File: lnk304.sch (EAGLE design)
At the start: 25 parts, among them IC2 MCP1703CB

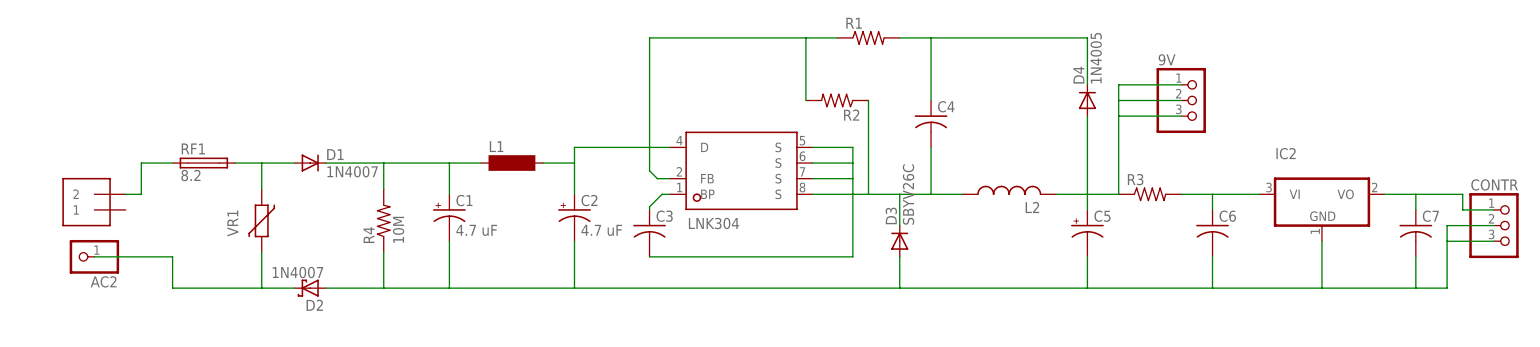
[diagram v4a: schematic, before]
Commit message: Added passive componets' values which were removed by mistake
** 27.Mar.2016 **

Schematic:
- Added passive componets' values which were removed by mistake

PCB Layout:
- Smash passive components and remove passive components' values

-- Missing --
- Need to add hot and neutral pins for AC plug concept
- Need to revise Terminal Block size and overlapping with D2
- May need to increase L2 pad distance a bit
- May need to decrease the board height by 2mm
- Add Creepage between C1 and C2 pads
- Revise the two holes diameter and availability of screws
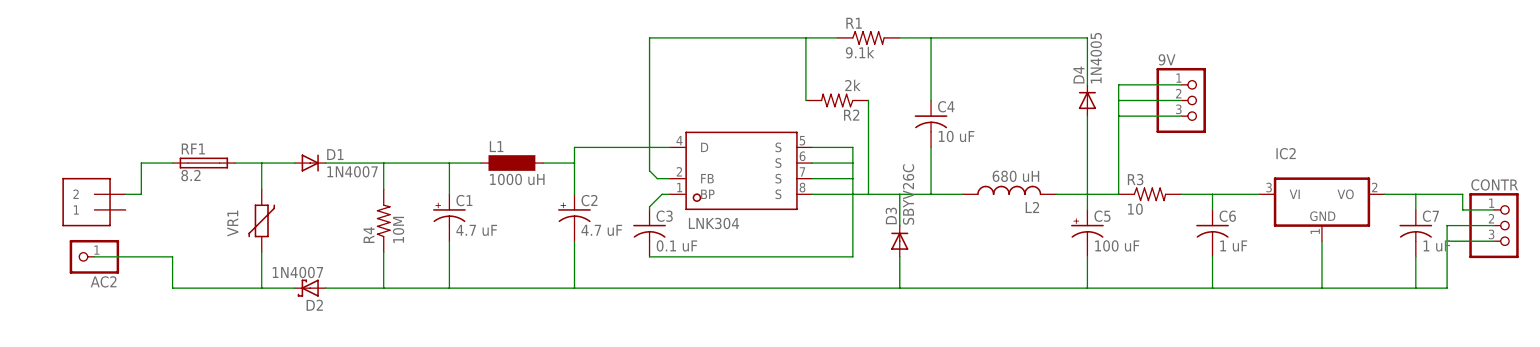
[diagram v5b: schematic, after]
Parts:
- C3: value (none) -> 0.1 uF
- C4: value (none) -> 10 uF
- C5: value (none) -> 100 uF
- C6, C7: value (none) -> 1 uF
- L1: value (none) -> 1000 uH
- L2: value (none) -> 680 uH
- R1: value (none) -> 9.1k
- R2: value (none) -> 2k
- R3: value (none) -> 10
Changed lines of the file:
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@@
 <part name="C1" library="adafruit" deviceset="CPOL-US" device="E5-10.5" value="4.7 uF"/>
 <part name="C2" library="adafruit" deviceset="CPOL-US" device="E5-10.5" value="4.7 uF"/>
-<part name="L1" library="inductor-neosid" deviceset="BS" device="11"/>
-<part name="C4" library="adafruit" deviceset="C-US" device="C0603"/>
-<part name="C3" library="adafruit" deviceset="C-US" device="C0603"/>
+<part name="L1" library="inductor-neosid" deviceset="BS" device="11" value="1000 uH"/>
+<part name="C4" library="adafruit" deviceset="C-US" device="C0603" value="10 uF"/>
+<part name="C3" library="adafruit" deviceset="C-US" device="C0603" value="0.1 uF"/>
 <part name="D3" library="adafruit" deviceset="1N4004" device="" value="SBYV26C"/>
 <part name="D4" library="adafruit" deviceset="1N4004" device="" value="1N4005"/>
-<part name="C5" library="adafruit" deviceset="CPOL-US" device="E2-4"/>
-<part name="L2" library="rcl" deviceset="L-US" device="L5650M"/>
-<part name="R1" library="adafruit" deviceset="R-US_" device="R0603"/>
-<part name="R2" library="adafruit" deviceset="R-US_" device="R0603"/>
+<part name="C5" library="adafruit" deviceset="CPOL-US" device="E2-4" value="100 uF"/>
+<part name="L2" library="rcl" deviceset="L-US" device="L5650M" value="680 uH"/>
+<part name="R1" library="adafruit" deviceset="R-US_" device="R0603" value="9.1k"/>
+<part name="R2" library="adafruit" deviceset="R-US_" device="R0603" value="2k"/>
 <part name="IC2" library="linear" deviceset="MCP1703" device="CB" value=""/>
-<part name="R3" library="adafruit" deviceset="R-US_" device="R1206"/>
-<part name="C6" library="adafruit" deviceset="C-US" device="C0603"/>
-<part name="C7" library="adafruit" deviceset="C-US" device="C0603"/>
+<part name="R3" library="adafruit" deviceset="R-US_" device="R1206" value="10"/>
+<part name="C6" library="adafruit" deviceset="C-US" device="C0603" value="1 uF"/>
+<part name="C7" library="adafruit" deviceset="C-US" device="C0603" value="1 uF"/>
 <part name="AC" library="adafruit" deviceset="1X2" device="-3.5MM"/>
 <part name="AC2" library="adafruit" deviceset="PINHD-1X1" device=""/>

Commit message: Create new PCB layout for AC TBlock and L2
** 8.Apr.2016 **
Created new devices in the library

Schematic:
- Created new library for AC plug
- Added hot and neutral pins for AC plug concept

PCB Layout:
- Revised Terminal Block size and overlapping with D2
- Probably won't need to decrease the board height by 2mm
- Neglect creepage between C1 and C2 pads at the moment
- Increased L2 pad distance a bit by creating a new library ELL-6UH681M
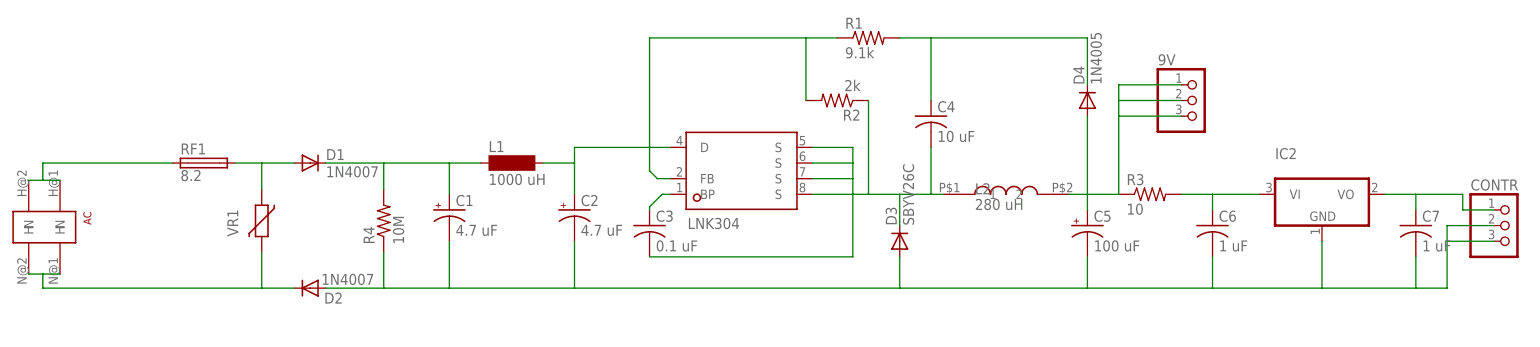
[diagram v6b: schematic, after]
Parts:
- removed AC2: (no value), adafruit:PINHD-1X1
- AC: value 1X2-3.5MM -> TBLOCK02X2; device adafruit:1X2-3.5MM -> userdefined:TBLOCK02X2
- D2: device adafruit:SCHOTTKY-DIODEDO41-7 -> adafruit:1N4004
- L2: value 680 uH -> 280 uH; device rcl:L-USL5650M -> userdefined:ELL-6UH681M
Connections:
- removed net N$9: AC.2, RF1.1
- new net N$12: AC.H@1, AC.H@2, RF1.1
- net N$6: now also AC.N@1, AC.N@2; no longer AC2.1
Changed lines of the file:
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@@
 <part name="RF1" library="fuse" deviceset="FUSE" device="PICOFUSE" value="8.2"/>
 <part name="D1" library="adafruit" deviceset="1N4004" device="" value="1N4007"/>
-<part name="D2" library="adafruit" deviceset="SCHOTTKY-DIODE" device="DO41-7" value="1N4007"/>
+<part name="D2" library="adafruit" deviceset="1N4004" device="" value="1N4007"/>
 <part name="C1" library="adafruit" deviceset="CPOL-US" device="E5-10.5" value="4.7 uF"/>
 <part name="C2" library="adafruit" deviceset="CPOL-US" device="E5-10.5" value="4.7 uF"/>
@@
 <part name="D4" library="adafruit" deviceset="1N4004" device="" value="1N4005"/>
 <part name="C5" library="adafruit" deviceset="CPOL-US" device="E2-4" value="100 uF"/>
-<part name="L2" library="rcl" deviceset="L-US" device="L5650M" value="680 uH"/>
 <part name="R1" library="adafruit" deviceset="R-US_" device="R0603" value="9.1k"/>
 <part name="R2" library="adafruit" deviceset="R-US_" device="R0603" value="2k"/>
@@
 <part name="C6" library="adafruit" deviceset="C-US" device="C0603" value="1 uF"/>
 <part name="C7" library="adafruit" deviceset="C-US" device="C0603" value="1 uF"/>
-<part name="AC" library="adafruit" deviceset="1X2" device="-3.5MM"/>
-<part name="AC2" library="adafruit" deviceset="PINHD-1X1" device=""/>
 <part name="CONTR" library="adafruit" deviceset="PINHD-1X3" device=""/>
 <part name="9V" library="adafruit" deviceset="PINHD-1X3" device=""/>
@@
 <part name="R4" library="resistor" deviceset="R-US_" device="R1206" value="10M"/>
 <part name="VR1" library="varistor" deviceset="VARISTOR" device="-7,5" value=""/>
+<part name="AC" library="userdefined" deviceset="TBLOCK02X2" device=""/>
+<part name="L2" library="userdefined" deviceset="ELL-6UH681M" device="" value="280 uH"/>
 </parts>
 <sheets>
@@
 <instance part="RF1" gate="G$1" x="0.508" y="60.96"/>
 <instance part="D1" gate="1" x="17.78" y="60.96"/>
-<instance part="D2" gate="G$1" x="17.78" y="40.64" rot="R180"/>
+<instance part="D2" gate="1" x="17.78" y="40.64" smashed="yes" rot="R180">
+<attribute name="NAME" x="23.114" y="39.9034" size="1.778" layer="95" rot="R180"/>
+<attribute name="VALUE" x="28.194" y="42.9514" size="1.778" layer="96" rot="R180"/>
+</instance>
 <instance part="C1" gate="G$1" x="40.386" y="53.34"/>
 <instance part="C2" gate="G$1" x="60.706" y="53.34"/>
@@
 <instance part="D4" gate="1" x="144.018" y="71.12" rot="R90"/>
 <instance part="C5" gate="G$1" x="144.018" y="50.8"/>
-<instance part="L2" gate="G$1" x="131.318" y="55.88" rot="R90"/>
 <instance part="R1" gate="G$1" x="108.458" y="81.28"/>
 <instance part="R2" gate="G$1" x="103.378" y="71.12" rot="R180"/>
@@
 <instance part="C6" gate="G$1" x="164.338" y="50.8"/>
 <instance part="C7" gate="G$1" x="197.358" y="50.8"/>
-<instance part="AC" gate="G$1" x="-17.272" y="55.88" rot="R180"/>
-<instance part="AC2" gate="G$1" x="-19.812" y="45.72" rot="R180"/>
 <instance part="CONTR" gate="A" x="212.598" y="50.8"/>
 <instance part="9V" gate="A" x="161.798" y="71.12"/>
@@
 <instance part="R4" gate="G$1" x="29.718" y="51.562" rot="R90"/>
 <instance part="VR1" gate="G$1" x="9.906" y="51.562" rot="R90"/>
+<instance part="AC" gate="G$1" x="-25.4" y="50.546" rot="R270"/>
+<instance part="L2" gate="G$1" x="130.81" y="55.88"/>
 </instances>
 <busses>
@@
 <net name="N$6" class="0">
 <segment>
-<pinref part="D2" gate="G$1" pin="C"/>
+<pinref part="D2" gate="1" pin="C"/>
 <wire x1="15.24" y1="40.64" x2="9.906" y2="40.64" width="0.1524" layer="91"/>
-<pinref part="AC2" gate="G$1" pin="1"/>
-<wire x1="9.906" y1="40.64" x2="-4.572" y2="40.64" width="0.1524" layer="91"/>
-<wire x1="-17.272" y1="45.72" x2="-4.572" y2="45.72" width="0.1524" layer="91"/>
-<wire x1="-4.572" y1="45.72" x2="-4.572" y2="40.64" width="0.1524" layer="91"/>
 <pinref part="VR1" gate="G$1" pin="2"/>
 <wire x1="9.906" y1="46.482" x2="9.906" y2="40.64" width="0.1524" layer="91"/>
+<wire x1="-25.654" y1="40.64" x2="9.906" y2="40.64" width="0.1524" layer="91"/>
+<pinref part="AC" gate="G$1" pin="N@2"/>
+<pinref part="AC" gate="G$1" pin="N@1"/>
+<wire x1="-22.86" y1="42.926" x2="-25.654" y2="42.926" width="0.1524" layer="91"/>
+<wire x1="-25.654" y1="42.926" x2="-27.94" y2="42.926" width="0.1524" layer="91"/>
+<wire x1="-25.654" y1="40.64" x2="-25.654" y2="42.926" width="0.1524" layer="91"/>
 </segment>
 </net>
@@
 <segment>
 <pinref part="D3" gate="1" pin="A"/>
-<pinref part="D2" gate="G$1" pin="A"/>
+<pinref part="D2" gate="1" pin="A"/>
 <pinref part="C2" gate="G$1" pin="-"/>
 <wire x1="60.706" y1="48.26" x2="60.706" y2="40.64" width="0.1524" layer="91"/>
@@
 <net name="N$4" class="0">
 <segment>
-<pinref part="L2" gate="G$1" pin="2"/>
 <pinref part="C5" gate="G$1" pin="+"/>
-<wire x1="138.938" y1="55.88" x2="144.018" y2="55.88" width="0.1524" layer="91"/>
 <wire x1="144.018" y1="55.88" x2="144.018" y2="53.34" width="0.1524" layer="91"/>
 <pinref part="D4" gate="1" pin="A"/>
@@
 <pinref part="9V" gate="A" pin="3"/>
 <wire x1="149.098" y1="68.58" x2="159.258" y2="68.58" width="0.1524" layer="91"/>
+<pinref part="L2" gate="G$1" pin="2"/>
+<wire x1="144.018" y1="55.88" x2="140.97" y2="55.88" width="0.1524" layer="91"/>
 </segment>
 </net>
@@
 <wire x1="108.458" y1="71.12" x2="108.458" y2="55.88" width="0.1524" layer="91"/>
 <pinref part="C4" gate="G$1" pin="2"/>
-<pinref part="L2" gate="G$1" pin="1"/>
-<wire x1="123.698" y1="55.88" x2="118.618" y2="55.88" width="0.1524" layer="91"/>
 <wire x1="118.618" y1="55.88" x2="118.618" y2="63.5" width="0.1524" layer="91"/>
 <pinref part="D3" gate="1" pin="C"/>
@@
 <pinref part="LNK304" gate="G$1" pin="S@2"/>
 <wire x1="99.314" y1="60.96" x2="105.918" y2="60.96" width="0.1524" layer="91"/>
+<pinref part="L2" gate="G$1" pin="1"/>
+<wire x1="120.65" y1="55.88" x2="118.618" y2="55.88" width="0.1524" layer="91"/>
 </segment>
 </net>
@@
 </segment>
 </net>
-<net name="N$9" class="0">
-<segment>
-<pinref part="AC" gate="G$1" pin="2"/>
-<wire x1="-12.192" y1="55.88" x2="-9.652" y2="55.88" width="0.1524" layer="91"/>
-<wire x1="-9.652" y1="55.88" x2="-9.652" y2="60.96" width="0.1524" layer="91"/>
-<pinref part="RF1" gate="G$1" pin="1"/>
-<wire x1="-9.652" y1="60.96" x2="-4.572" y2="60.96" width="0.1524" layer="91"/>
-</segment>
-</net>
 <net name="N$7" class="0">
 <segment>
@@
 </segment>
 </net>
+<net name="N$12" class="0">
+<segment>
+<pinref part="AC" gate="G$1" pin="H@1"/>
+<pinref part="AC" gate="G$1" pin="H@2"/>
+<wire x1="-27.94" y1="58.166" x2="-25.654" y2="58.166" width="0.1524" layer="91"/>
+<pinref part="RF1" gate="G$1" pin="1"/>
+<wire x1="-25.654" y1="58.166" x2="-22.86" y2="58.166" width="0.1524" layer="91"/>
+<wire x1="-25.654" y1="58.166" x2="-25.654" y2="60.96" width="0.1524" layer="91"/>
+<wire x1="-25.654" y1="60.96" x2="-4.572" y2="60.96" width="0.1524" layer="91"/>
+</segment>
+</net>
 </nets>
 </sheet>
@@
 </schematic>
 </drawing>
+<compatibility>
+<note version="6.3" minversion="6.2.2" severity="warning">
+Since Version 6.2.2 text objects can contain more than one line,
+which will not be processed correctly with this version.
+</note>
+</compatibility>
 </eagle>
